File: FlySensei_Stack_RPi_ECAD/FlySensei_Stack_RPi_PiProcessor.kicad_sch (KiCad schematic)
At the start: 25 parts, among them J1 Conn_01x03, Q1 Q_NMOS_GSD, SW1 SW_SPST, U1 ComputeModule4-CM4, U2 ATtiny85V-10S, U3 74LVC1G07

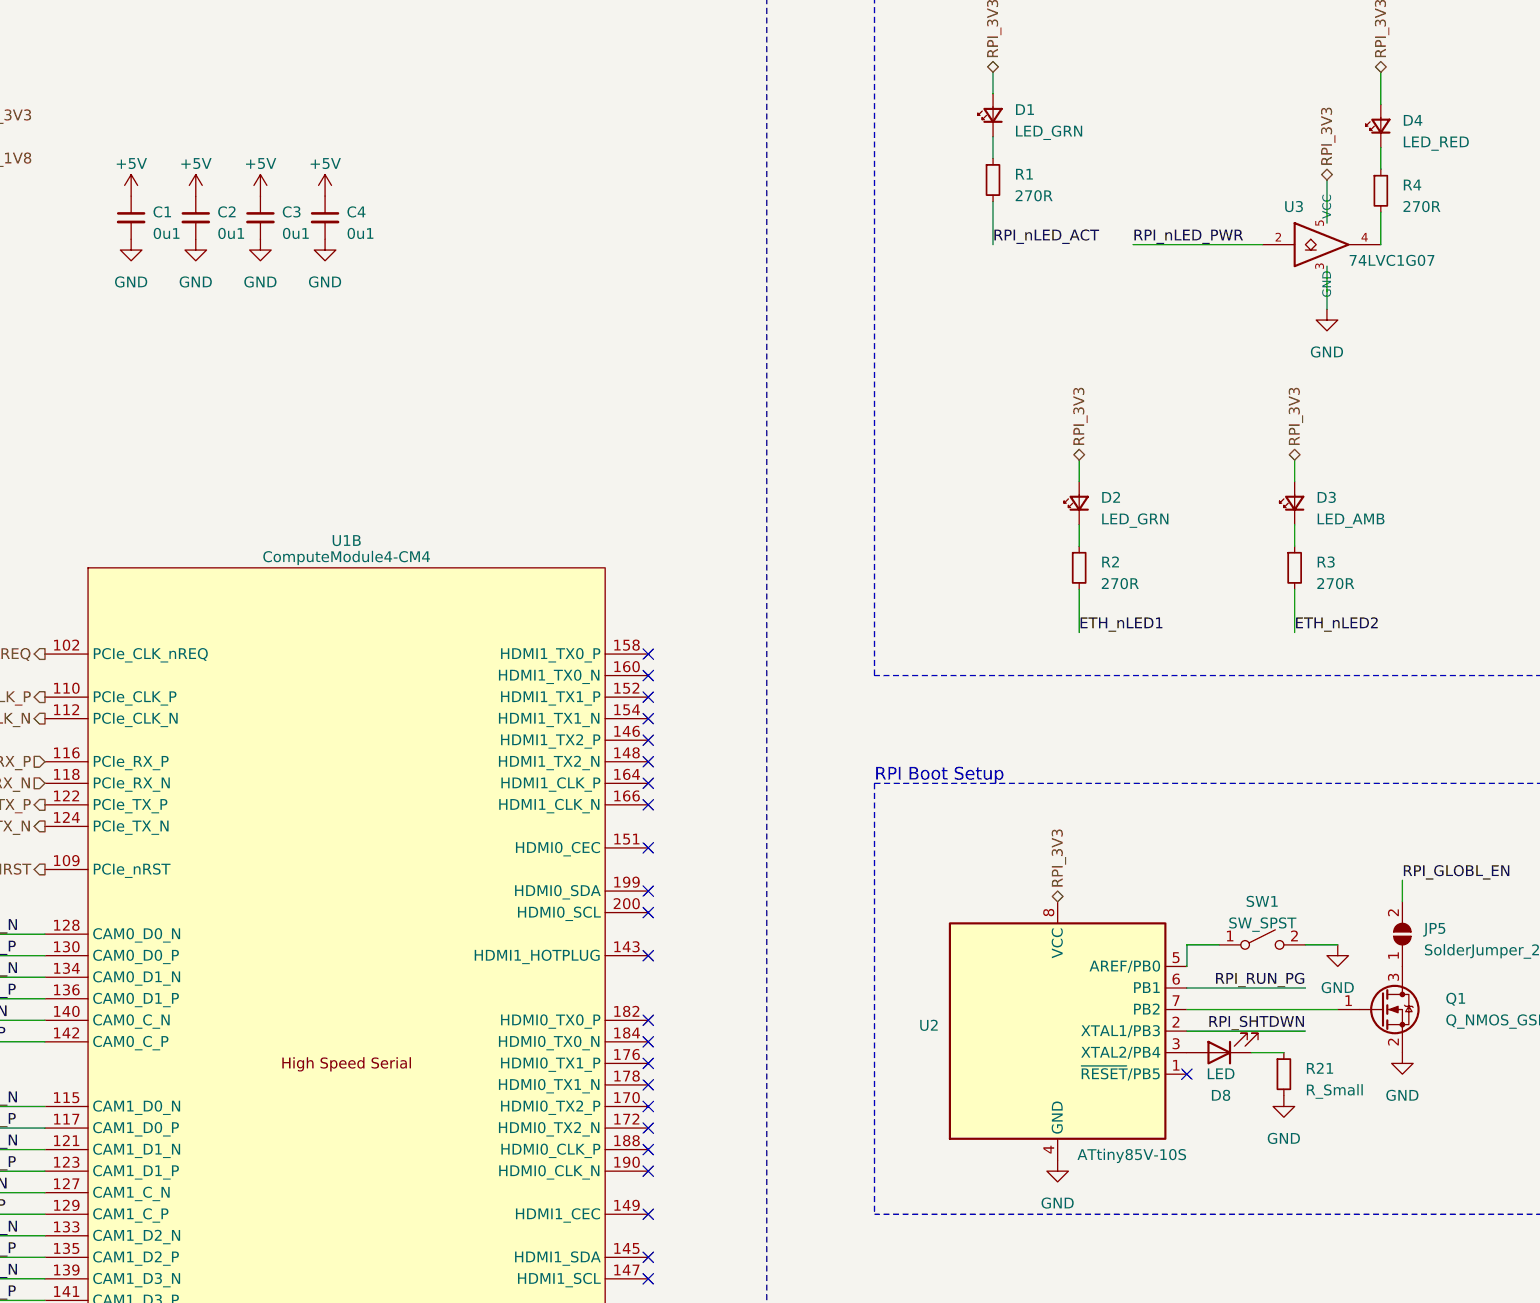
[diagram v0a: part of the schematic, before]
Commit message: PCB Design for the Raspberry PI CM4 Board (V0.1)
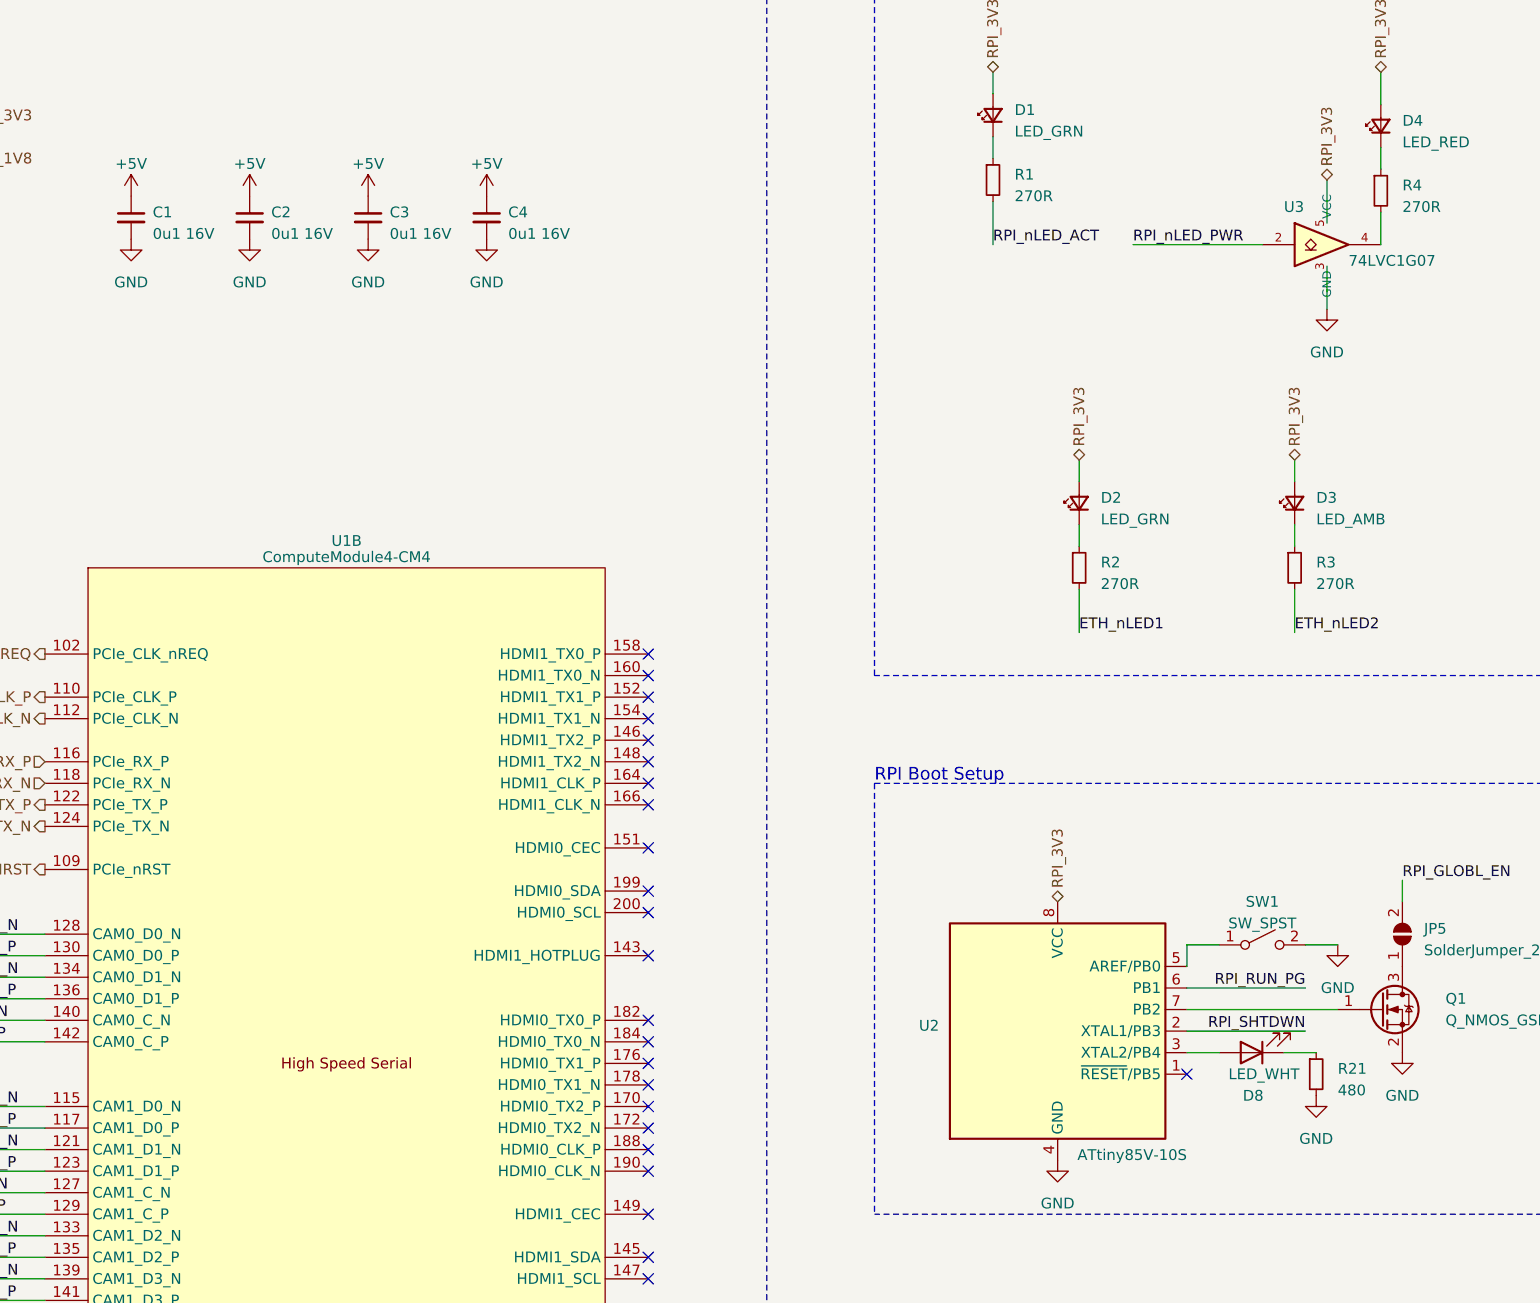
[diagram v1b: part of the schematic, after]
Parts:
- C1, C2, C3, C4: value 0u1 -> 0u1 16V; footprint (none) -> Capacitor_SMD:C_0402_1005Metric
- D1, D2, D3, D4: footprint (none) -> LED_SMD:LED_0603_1608Metric
- D8: value LED -> LED_WHT; footprint (none) -> LED_SMD:LED_0603_1608Metric
- J1: footprint (none) -> Connector_PinHeader_1.00mm:PinHeader_1x03_P1.00mm_Vertical
- JP1, JP2, JP3, JP4, JP5: footprint (none) -> Jumper:SolderJumper-2_P1.3mm_Open_RoundedPad1.0x1.5mm
- R1, R2, R3, R4: footprint (none) -> Resistor_SMD:R_0402_1005Metric
- R21: value R_Small -> 480; footprint (none) -> Resistor_SMD:R_0402_1005Metric
- SW1: footprint (none) -> Button_Switch_SMD:Panasonic_EVQPUL_EVQPUC
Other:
- moved on the sheet: C2, C3, C4, D8, R21

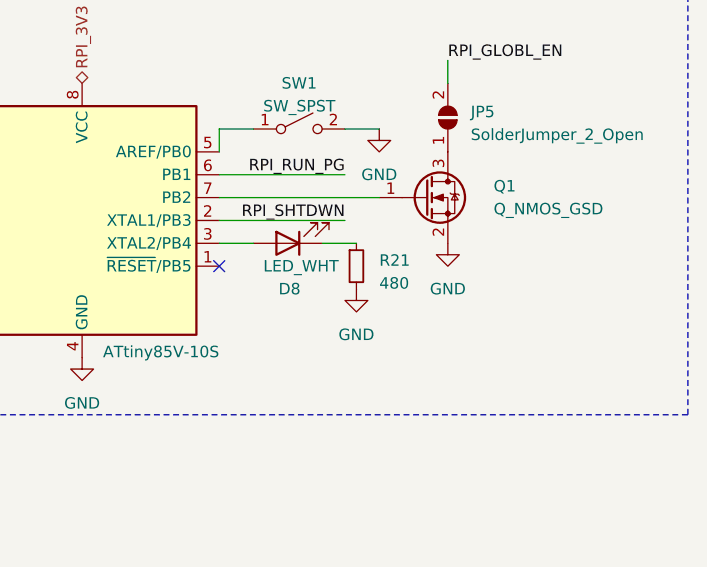
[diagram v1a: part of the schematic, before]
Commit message: Cleanup component values to remain consistent in all skeets
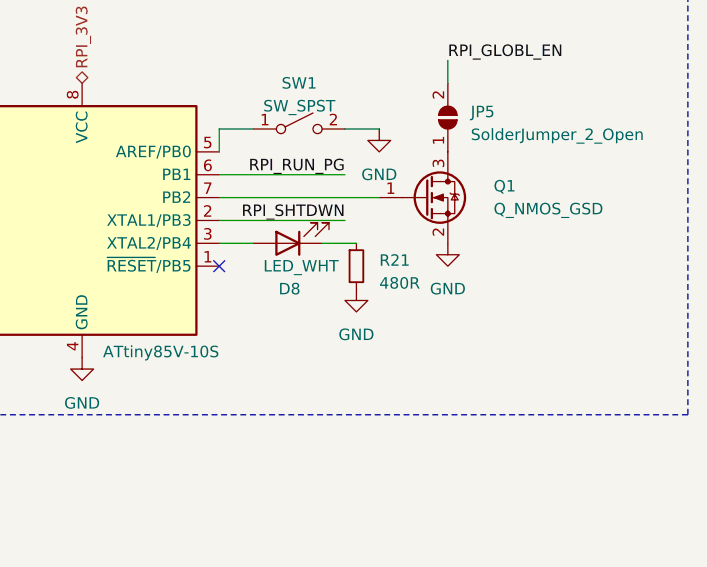
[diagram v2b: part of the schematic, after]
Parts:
- R21: value 480 -> 480R
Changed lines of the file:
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@@
       (effects (font (size 1.27 1.27)) (justify left))
     )
-    (property "Value" "480" (id 1) (at 372.11 163.1949 0)
+    (property "Value" "480R" (id 1) (at 372.11 163.1949 0)
       (effects (font (size 1.27 1.27)) (justify left))
     )
